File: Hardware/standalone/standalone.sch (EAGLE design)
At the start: 92 parts, among them IC1 STM32F050C6T6A, IC2 AP1212, Q2 32.768khz, U1 DMS3016SSS-13, U2 DMS3016SSS-13, U3 DMS3016SSS-13, U4 LM2576S, U5 NMOS_2N7002, U6 NMOS_2N7002, X1 KUSBVX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

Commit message: Major PCB Re-arrangements and Fixes
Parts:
- RSENSE2, RSENSE_BATT: value 0.005 -> 0.1
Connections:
- net CC_~EN renamed CC_EN
- removed net N$9: C10.1, C11.2, C4.+, D2.A, GATE_DRIVE.VCC, R1.2, RSENSE2.2, SENSE_AMP_SOL.S-, U1.S, U1.S_2, U1.S_3
- new net N$38: RSENSE2.1, SENSE_AMP_SOL.S+, SOL.3
- net N$16: now also C10.1, C11.2, C4.+, D2.A, GATE_DRIVE.VCC, R1.2, RSENSE2.2, SENSE_AMP_SOL.S-, U1.S, U1.S_2, U1.S_3; no longer RSENSE2.1, SENSE_AMP_SOL.S+, SOL.3
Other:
- note added: "TODO: - Battery Bi-Directional Current Sense - Change Current Sense R - Check if LCD R/W Pin is needed? - Add filtering (LC) to AVCC - Remove U1 (Not needed) - Place Keep-out border around the edge of board - Contrast Adjust Pot needs changing"
- note added: "Use Internal Pull Ups"
- note removed: "TODO: - Battery Bi-Directional Current Sense - Change Current Sense R - Check if LCD R/W Pin is needed? - Add filtering (LC) to AVCC - Change Inductors and Cap for Buck - Remove U1 (Not needed) - Change Power Switch - Place Keep-out border around the edge of board - Contrast Adjust Pot needs changing"
- moved on the sheet: C19, C7, R3, R4, RSENSE2, R_GAIN, SENSE_AMP_SOL

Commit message: PCB 100% Routed
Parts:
- C20: value 10uF -> 1uF
- C8: value 1uF -> 10uF
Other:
- note added: "TODO: - Battery Bi-Directional Current Sense - Change Current Sense R - Check if LCD R/W Pin is needed? - Add filtering (LC) to AVCC - Remove U1 (Not needed) - Place Keep-out border around the edge of board - Contrast Adjust Pot needs changing - Change Batt Current sense to INA2 Series"
- note removed: "TODO: - Battery Bi-Directional Current Sense - Change Current Sense R - Check if LCD R/W Pin is needed? - Add filtering (LC) to AVCC - Remove U1 (Not needed) - Place Keep-out border around the edge of board - Contrast Adjust Pot needs changing"

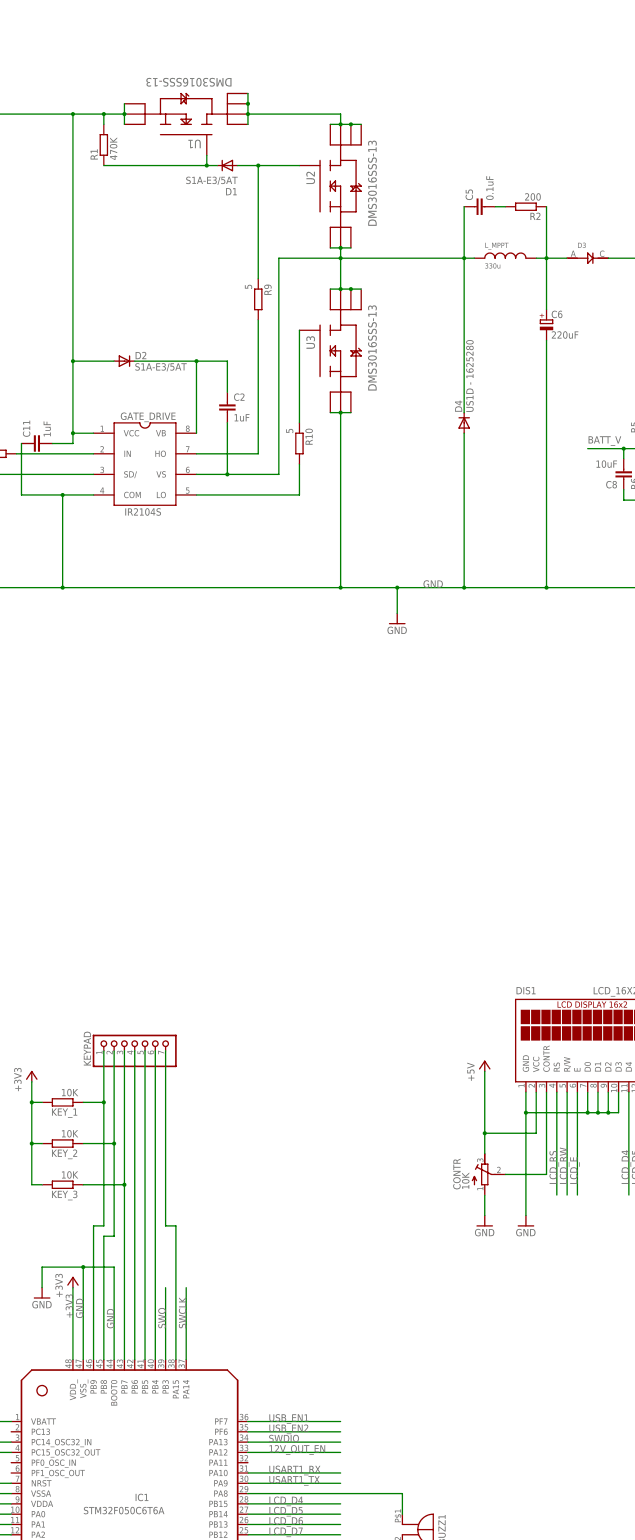
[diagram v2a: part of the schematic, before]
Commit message: PCB Fixes
LCD Power Switch Added.
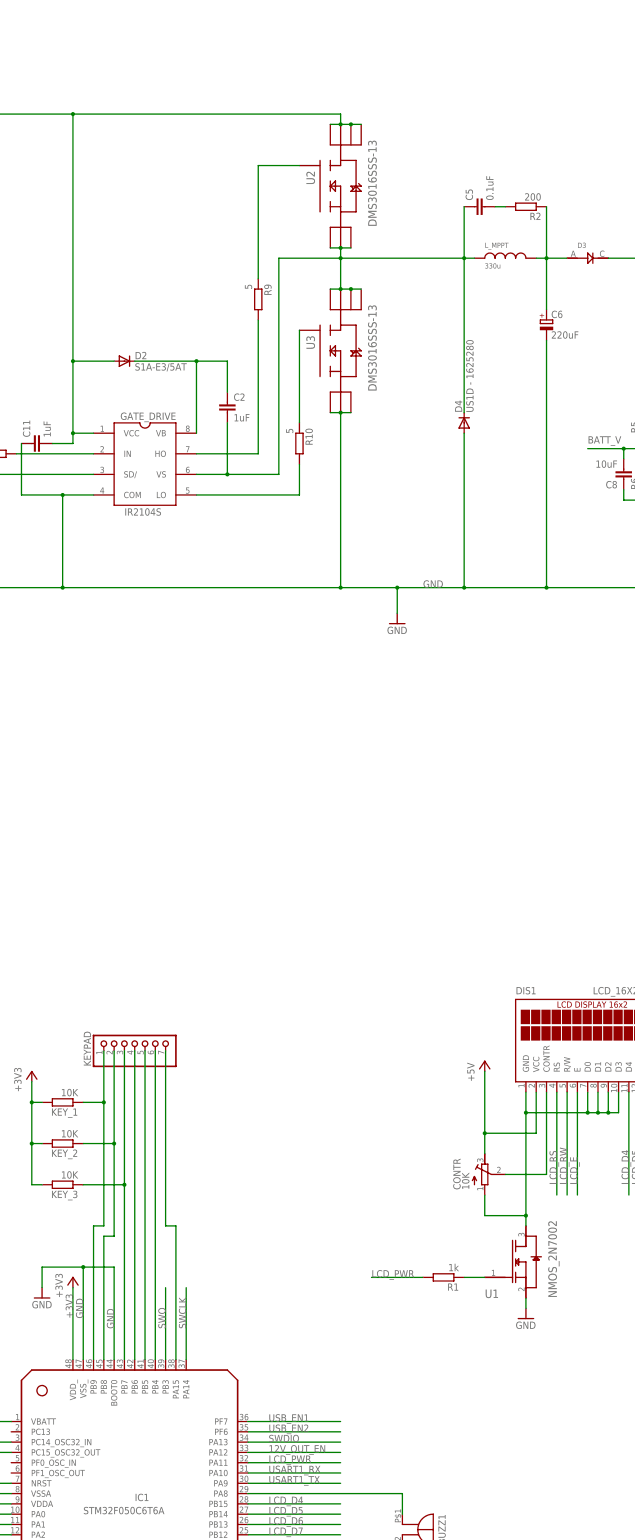
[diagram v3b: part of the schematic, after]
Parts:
- removed D1: S1A-E3/5AT, diode:DIODE-DO-214AC
- R1: value 470K -> 1k; device rcl:R-EU_M0805 -> resistor:R-EU_M0805
- U1: value DMS3016SSS-13 -> NMOS_2N7002; device equinox:DMS3016SSS-13 -> equinox:NMOS_2N7002; MPN (none) -> 2N7002-7-F; OC_FARNELL (none) -> 1713823; OC_NEWARK (none) -> 25R5679; PACKAGE (none) -> SOT-23-3; SUPPLIER (none) -> DIODES INC.
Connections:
- new net LCD_PWR: IC1.PA11, R1.2
- net GND: now also U1.S; no longer CONTR.E, DIS1.D0, DIS1.D1, DIS1.D2, DIS1.D3, DIS1.GND
- net N$14: no longer D1.A
- net N$16: now also U2.D, U2.D_2, U2.D_3, U2.D_4; no longer R1.2, U1.S, U1.S_2, U1.S_3
- net N$17: now also R1.1, U1.G; no longer U1.D, U1.D_2, U1.D_3, U1.D_4, U2.D, U2.D_2, U2.D_3, U2.D_4
- net N$5: now also CONTR.E, DIS1.D0, DIS1.D1, DIS1.D2, DIS1.D3, DIS1.GND, U1.D; no longer D1.C, R1.1, U1.G
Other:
- note added: "TODO: - Contrast Adjust Pot needs changing - Change Batt Current sense to INA2 Series"
- note removed: "TODO: - Battery Bi-Directional Current Sense - Change Current Sense R - Check if LCD R/W Pin is needed? - Add filtering (LC) to AVCC - Remove U1 (Not needed) - Place Keep-out border around the edge of board - Contrast Adjust Pot needs changing - Change Batt Current sense to INA2 Series"
- moved on the sheet: R1

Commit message: PCB Rev2  Complete. Ready for manufacture
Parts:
- removed RSENSE_BATT: 0.1, rcl:R-EU_R2512
- removed R_GAIN1: 1k65, rcl:R-EU_M0805
- removed SENSE_AMP_BATT: ZXCT1107SA-7, equinox:ZXCT1107SA-7
- added R25, R26: 10K, rcl:R-EU_M0805
- added R27, R28: 10, rcl:R-EU_M0805
- added RS_B: 0.01, rcl:R-EU_R2512
- added U7: INA213AIDCKT, equinox:INA213AIDCKT
- C20: value 1uF -> 10uF
- renumbered RSENSE2 to RS_S, R_GAIN to R30, SENSE_AMP_SOL to U10, U$9 to U9
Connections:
- new net N$39: R25.1, R26.2, U7.REF
- new net N$40: C20.2, R27.1, U7.IN+
- new net N$41: C20.1, R28.1, U7.IN-
- net +3V3: now also R25.2, U7.V+
- net BATT_I: now also U7.OUT; no longer C20.2, R_GAIN1.2, SENSE_AMP_BATT.OUT
- net GND: now also R26.1, U7.GND; no longer C20.1, R_GAIN1.1
- net N$4: now also R28.2, RS_B.2; no longer RSENSE_BATT.2, SENSE_AMP_BATT.S-
- net V_LOAD: now also R27.2, RS_B.1; no longer RSENSE_BATT.1, SENSE_AMP_BATT.S+
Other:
- note added: "TODO: - Contrast Adjust Pot needs changing"
- note removed: "TODO: - Contrast Adjust Pot needs changing - Change Batt Current sense to INA2 Series"
- moved on the sheet: BATTCON$1, BATTCON$2, C11, C2, C20, C5, C6, C8, D2, D3, D4, GATE_DRIVE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

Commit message: First Test of Keypad Code
Working but needs to be implemented with interrupts and de-bouncing

Hardware pull up resistors no longer required. Internal uC pull ups are
used.
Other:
- note added: "NP"
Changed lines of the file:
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@@
 <text x="297.18" y="66.04" size="1.778" layer="98">Must be 0placed near to IC1</text>
 <text x="165.1" y="193.04" size="1.778" layer="98" rot="R90">Use Internal Pull Ups</text>
+<text x="170.688" y="217.424" size="1.778" layer="98">NP</text>
+<text x="170.942" y="207.518" size="1.778" layer="98">NP</text>
+<text x="170.688" y="197.358" size="1.778" layer="98">NP</text>
 </plain>
 <instances>

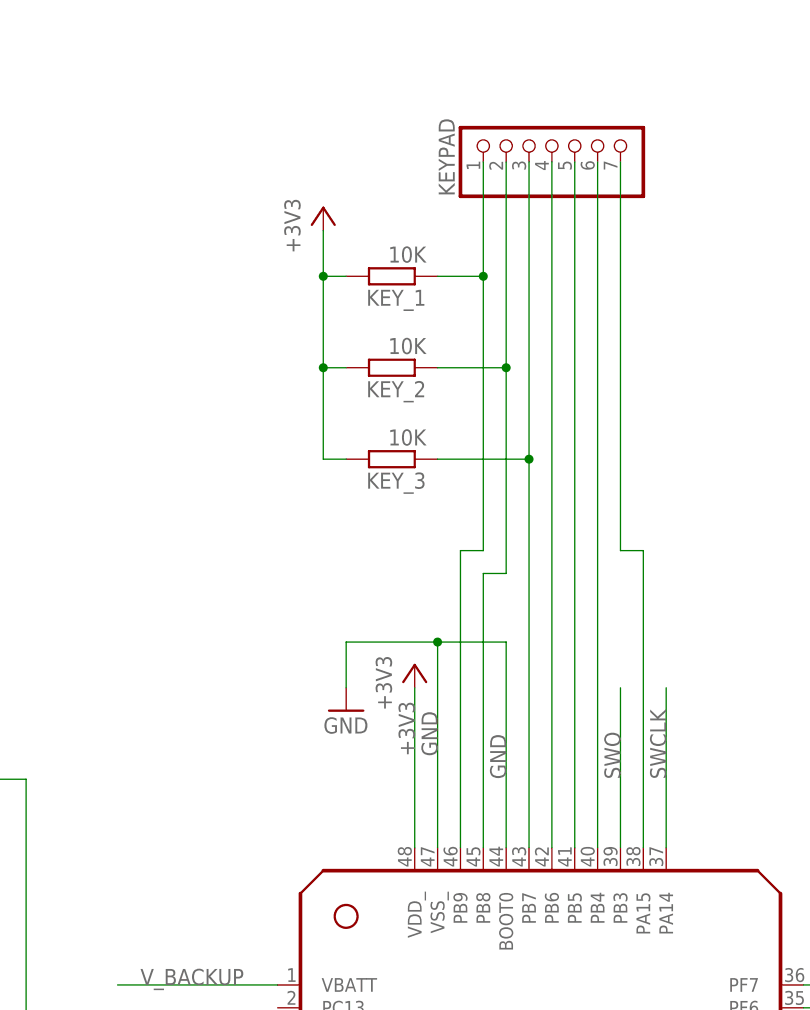
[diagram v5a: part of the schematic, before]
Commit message: Removed Keypad Pullups and Fixed MPPT out tracks
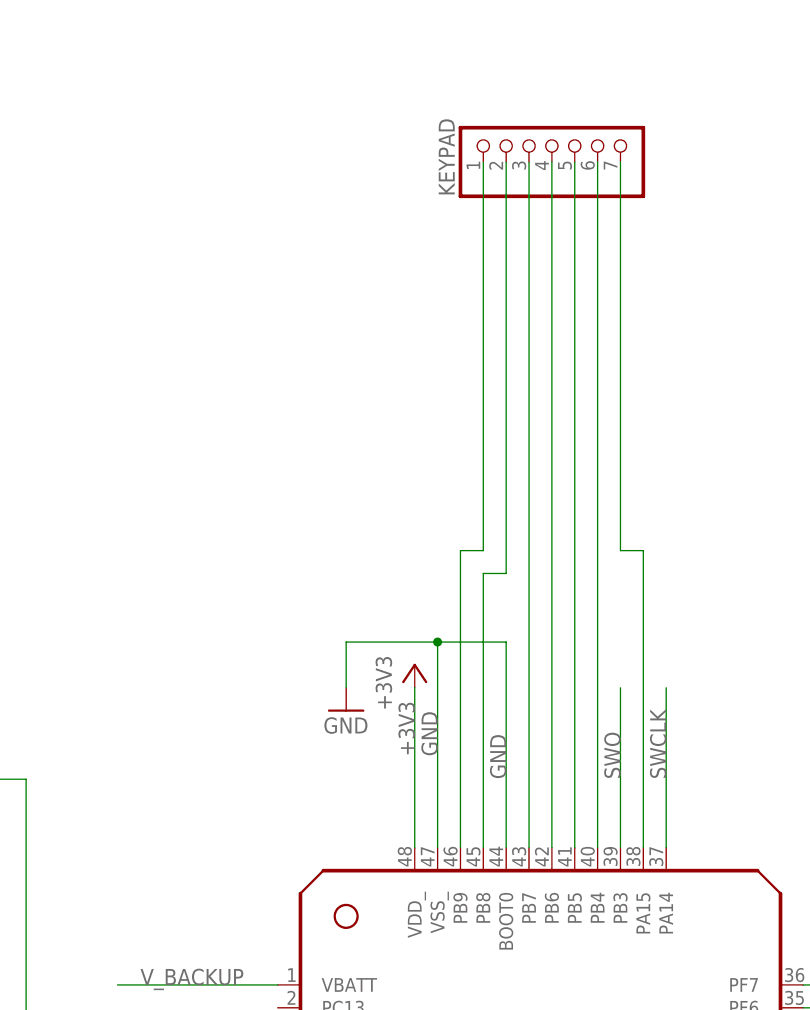
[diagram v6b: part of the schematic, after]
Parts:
- removed KEY_1, KEY_2, KEY_3: 10K, rcl:R-EU_M0805
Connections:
- net +3V3: no longer KEY_1.2, KEY_2.2, KEY_3.2
- net N$23: no longer KEY_1.1
- net N$24: no longer KEY_2.1
- net N$26: no longer KEY_3.1
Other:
- note removed: "NP"
- note removed: "Use Internal Pull Ups"
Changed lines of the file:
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@@
 <drawing>
 <settings>
-<setting alwaysvectorfont="no"/>
+<setting alwaysvectorfont="yes"/>
 <setting verticaltext="up"/>
 </settings>
@@
 <part name="GND17" library="supply1" deviceset="GND" device="" value="GND"/>
 <part name="KEYPAD" library="pinhead" deviceset="PINHD-1X7" device="/90"/>
-<part name="KEY_1" library="rcl" deviceset="R-EU_" device="M0805" value="10K"/>
-<part name="KEY_2" library="rcl" deviceset="R-EU_" device="M0805" value="10K"/>
-<part name="KEY_3" library="rcl" deviceset="R-EU_" device="M0805" value="10K"/>
-<part name="+3V7" library="supply1" deviceset="+3V3" device=""/>
 <part name="L_5V" library="equinox" deviceset="INDUC_BOURNES_SDR2207" device="" value="100uH"/>
 <part name="GND19" library="supply1" deviceset="GND" device="" value="GND"/>
@@
 <text x="556.26" y="132.08" size="1.778" layer="98" rot="R90">250mA Output</text>
 <text x="297.18" y="66.04" size="1.778" layer="98">Must be 0placed near to IC1</text>
-<text x="165.1" y="193.04" size="1.778" layer="98" rot="R90">Use Internal Pull Ups</text>
-<text x="170.688" y="217.424" size="1.778" layer="98">NP</text>
-<text x="170.942" y="207.518" size="1.778" layer="98">NP</text>
-<text x="170.688" y="197.358" size="1.778" layer="98">NP</text>
 </plain>
 <instances>
@@
 <instance part="GND17" gate="1" x="259.08" y="99.06"/>
 <instance part="KEYPAD" gate="A" x="193.04" y="231.14" rot="R90"/>
-<instance part="KEY_1" gate="G$1" x="175.26" y="215.9" rot="R180"/>
-<instance part="KEY_2" gate="G$1" x="175.26" y="205.74" rot="R180"/>
-<instance part="KEY_3" gate="G$1" x="175.26" y="195.58" rot="R180"/>
-<instance part="+3V7" gate="G$1" x="167.64" y="223.52"/>
 <instance part="L_5V" gate="1" x="525.78" y="66.04"/>
 <instance part="GND19" gate="1" x="467.36" y="33.02"/>
@@
 </segment>
 <segment>
-<pinref part="+3V7" gate="G$1" pin="+3V3"/>
-<pinref part="KEY_1" gate="G$1" pin="2"/>
-<wire x1="167.64" y1="220.98" x2="167.64" y2="215.9" width="0.1524" layer="91"/>
-<pinref part="KEY_2" gate="G$1" pin="2"/>
-<wire x1="167.64" y1="215.9" x2="170.18" y2="215.9" width="0.1524" layer="91"/>
-<wire x1="170.18" y1="205.74" x2="167.64" y2="205.74" width="0.1524" layer="91"/>
-<wire x1="167.64" y1="205.74" x2="167.64" y2="215.9" width="0.1524" layer="91"/>
-<junction x="167.64" y="215.9"/>
-<wire x1="167.64" y1="205.74" x2="167.64" y2="195.58" width="0.1524" layer="91"/>
-<junction x="167.64" y="205.74"/>
-<pinref part="KEY_3" gate="G$1" pin="2"/>
-<wire x1="167.64" y1="195.58" x2="170.18" y2="195.58" width="0.1524" layer="91"/>
-</segment>
-<segment>
 <pinref part="VREG" gate="A" pin="VOUT"/>
 <wire x1="505.46" y1="132.08" x2="518.16" y2="132.08" width="0.1524" layer="91"/>
@@
 <segment>
 <pinref part="KEYPAD" gate="A" pin="1"/>
-<wire x1="185.42" y1="228.6" x2="185.42" y2="215.9" width="0.1524" layer="91"/>
-<pinref part="KEY_1" gate="G$1" pin="1"/>
-<wire x1="185.42" y1="215.9" x2="185.42" y2="185.42" width="0.1524" layer="91"/>
-<wire x1="180.34" y1="215.9" x2="185.42" y2="215.9" width="0.1524" layer="91"/>
-<junction x="185.42" y="215.9"/>
+<wire x1="185.42" y1="228.6" x2="185.42" y2="185.42" width="0.1524" layer="91"/>
 <wire x1="185.42" y1="185.42" x2="182.88" y2="185.42" width="0.1524" layer="91"/>
 <pinref part="IC1" gate="1" pin="PB9"/>
@@
 <segment>
 <pinref part="KEYPAD" gate="A" pin="2"/>
-<wire x1="187.96" y1="228.6" x2="187.96" y2="205.74" width="0.1524" layer="91"/>
-<pinref part="KEY_2" gate="G$1" pin="1"/>
-<wire x1="187.96" y1="205.74" x2="187.96" y2="182.88" width="0.1524" layer="91"/>
-<wire x1="180.34" y1="205.74" x2="187.96" y2="205.74" width="0.1524" layer="91"/>
-<junction x="187.96" y="205.74"/>
+<wire x1="187.96" y1="228.6" x2="187.96" y2="182.88" width="0.1524" layer="91"/>
 <pinref part="IC1" gate="1" pin="PB8"/>
 <wire x1="185.42" y1="152.4" x2="185.42" y2="182.88" width="0.1524" layer="91"/>
@@
 <segment>
 <pinref part="KEYPAD" gate="A" pin="3"/>
-<wire x1="190.5" y1="228.6" x2="190.5" y2="195.58" width="0.1524" layer="91"/>
-<pinref part="KEY_3" gate="G$1" pin="1"/>
-<wire x1="180.34" y1="195.58" x2="190.5" y2="195.58" width="0.1524" layer="91"/>
-<junction x="190.5" y="195.58"/>
 <pinref part="IC1" gate="1" pin="PB7"/>
-<wire x1="190.5" y1="152.4" x2="190.5" y2="195.58" width="0.1524" layer="91"/>
-</segment>
-</net>
+<wire x1="190.5" y1="152.4" x2="190.5" y2="228.6" width="0.1524" layer="91"/>
+</segment>
+</net>

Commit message: Updated MPPT Inductor and added comments
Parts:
- 5V_CIN: value 100u -> 100uF; OC_FARNELL (none) -> 1539489
- 5V_COUT: OC_FARNELL (none) -> 1244342
- BATT: OC_FARNELL (none) -> 1012166
- BATT_BCKUP: OC_FARNELL (none) -> 1298246
- BUZZ1: OC_FARNELL (none) -> 1669967
- C4: OC_FARNELL (none) -> 1539489
- C5: value 0.1uF -> 100nF
- C6: OC_FARNELL (none) -> 9695877
- D2: OC_FARNELL (none) -> 9550216
- D3: value (none) -> SSB43L; OC_FARNELL (none) -> 1336556
- D4: value US1D - 1625280 -> US1D; OC_FARNELL (none) -> 1625280
- D6: OC_FARNELL (none) -> 1843695
- GATE_DRIVE: OC_FARNELL (none) -> 8638756
- IC1: OC_FARNELL (none) -> 2115059
- IC2: OC_FARNELL (none) -> 1825302
- KEYPAD: OC_FARNELL (none) -> 588763
- L_5V: OC_FARNELL (none) -> 1612709
- L_MPPT: OC_FARNELL (none) -> 1929706
- Q2: OC_FARNELL (none) -> 2101358
- R21: value 1K -> 1k
- SOL: TOBY (none) -> DC-001-A-2.1mm-R
- U$2, U$3, U$4: TOBY (none) -> DC-031-B
- U2, U3: value DMS3016SSS-13 -> FDS6690a; OC_FARNELL (none) -> 9845275
- U4: OC_FARNELL (none) -> 1469178
- U9: OC_FARNELL (none) -> 1525544
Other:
- note added: "0.5A Current Limit"
- note added: "Add PTC: 1800724 And Diode"
- note added: "Swap with 1192513"
- note added: "TODO: - Contrast Adjust Pot needs changing - Add PTC & Diode - Change Buzzer and add mosfet switching for higher voltage, thus louder"
- note removed: "1A Current Limit"
- note removed: "TODO: - Contrast Adjust Pot needs changing"
- moved on the sheet: C19, R30, RS_S, U10
